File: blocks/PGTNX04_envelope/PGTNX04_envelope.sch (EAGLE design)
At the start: 71 parts, among them IC1 TL084P, IC2 AS3310

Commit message: Committed a load of changes
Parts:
- added STN2: HEADER/MALE/01, connectors:HEADER/MALE/01
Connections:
- new net N$32: R11.S, STN2.3
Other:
- note added: "Connect to STNCV"
- note added: "From STNCV input jack normalled to +V"
- moved on the sheet: R11, R32, STN1, STN3
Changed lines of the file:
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@@
+<attribute name="SPICEPREFIX" value="X"/>
+</part>
+<part name="STN2" library="connectors" deviceset="HEADER/MALE/01" device="">
 <attribute name="SPICEPREFIX" value="X"/>
 </part>
@@
 <sheet>
 <plain>
+<text x="161.29" y="-22.098" size="1.778" layer="95">Connect to STNCV</text>
+<text x="208.28" y="-12.7" size="1.778" layer="95">From STNCV input jack normalled to +V</text>
 </plain>
 <instances>
@@
 <instance part="SUPPLY11" gate="GND" x="55.88" y="-91.44"/>
 <instance part="DCYCV" gate="HEADER" x="83.82" y="-60.96"/>
-<instance part="R11" gate="G$1" x="165.1" y="-17.78" rot="R180"/>
-<instance part="SUPPLY17" gate="GND" x="165.1" y="-27.94"/>
+<instance part="R11" gate="G$1" x="187.96" y="-17.78" rot="R180"/>
+<instance part="SUPPLY17" gate="GND" x="187.96" y="-27.94"/>
 <instance part="STNCV" gate="HEADER" x="152.4" y="-15.24" rot="R270"/>
-<instance part="SUPPLY18" gate="+12V" x="165.1" y="5.08"/>
+<instance part="SUPPLY18" gate="+12V" x="187.96" y="5.08"/>
 <instance part="GATE" gate="HEADER" x="48.26" y="-7.62"/>
 <instance part="GATEN" gate="HEADER" x="48.26" y="-5.08"/>
@@
 <instance part="ATK2" gate="HEADER" x="71.12" y="-190.5" rot="R90"/>
 <instance part="ATK3" gate="HEADER" x="53.34" y="-193.04"/>
-<instance part="R32" gate="G$1" x="165.1" y="-5.08" rot="R90"/>
-<instance part="STN1" gate="HEADER" x="167.64" y="-22.86" rot="R180"/>
-<instance part="STN3" gate="HEADER" x="167.64" y="-12.7" rot="R180"/>
+<instance part="R32" gate="G$1" x="187.96" y="-5.08" rot="R90"/>
+<instance part="STN1" gate="HEADER" x="190.5" y="-22.86" rot="R180"/>
+<instance part="STN3" gate="HEADER" x="190.5" y="-12.7" rot="R180"/>
+<instance part="STN2" gate="HEADER" x="180.34" y="-17.78"/>
 </instances>
 <busses>
@@
 <pinref part="R11" gate="G$1" pin="A"/>
 <pinref part="SUPPLY17" gate="GND" pin="PE"/>
-<wire x1="165.1" y1="-25.4" x2="165.1" y2="-22.86" width="0.1524" layer="91"/>
+<wire x1="187.96" y1="-25.4" x2="187.96" y2="-22.86" width="0.1524" layer="91"/>
 <pinref part="STN1" gate="HEADER" pin="3"/>
-<junction x="165.1" y="-22.86"/>
+<junction x="187.96" y="-22.86"/>
 </segment>
 <segment>
@@
 <pinref part="SUPPLY18" gate="+12V" pin="+12V"/>
 <pinref part="R32" gate="G$1" pin="2"/>
-<wire x1="165.1" y1="2.54" x2="165.1" y2="0" width="0.1524" layer="91"/>
+<wire x1="187.96" y1="2.54" x2="187.96" y2="0" width="0.1524" layer="91"/>
 </segment>
 </net>
@@
 <pinref part="R11" gate="G$1" pin="E"/>
 <pinref part="R32" gate="G$1" pin="1"/>
-<wire x1="165.1" y1="-10.16" x2="165.1" y2="-12.7" width="0.1524" layer="91"/>
+<wire x1="187.96" y1="-10.16" x2="187.96" y2="-12.7" width="0.1524" layer="91"/>
 <pinref part="STN3" gate="HEADER" pin="3"/>
-<junction x="165.1" y="-12.7"/>
-</segment>
-</net>
+<junction x="187.96" y="-12.7"/>
+</segment>
+</net>
+<net name="N$32" class="0">
+<segment>
+<pinref part="R11" gate="G$1" pin="S"/>
+<pinref part="STN2" gate="HEADER" pin="3"/>
+</segment>
+</net>

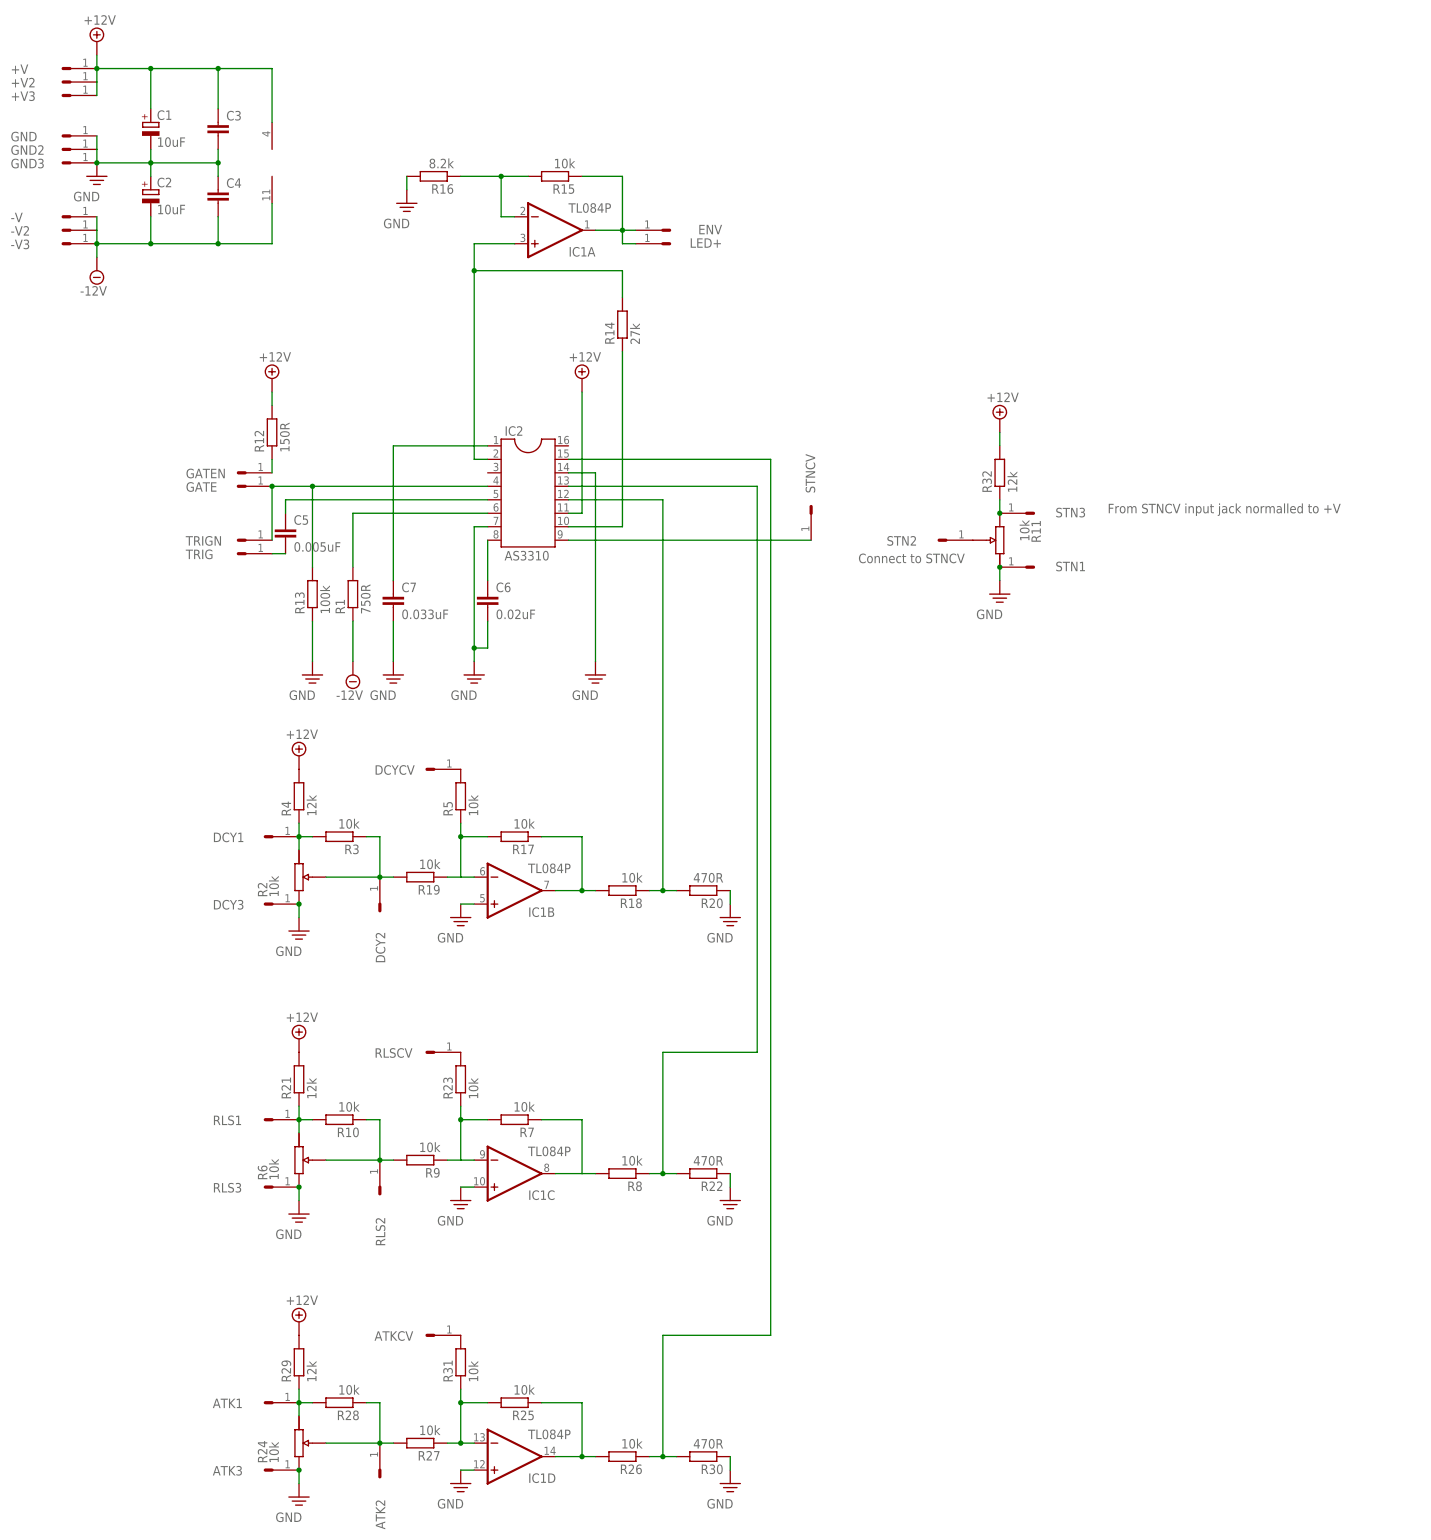
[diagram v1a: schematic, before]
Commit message: Corrected resistor value
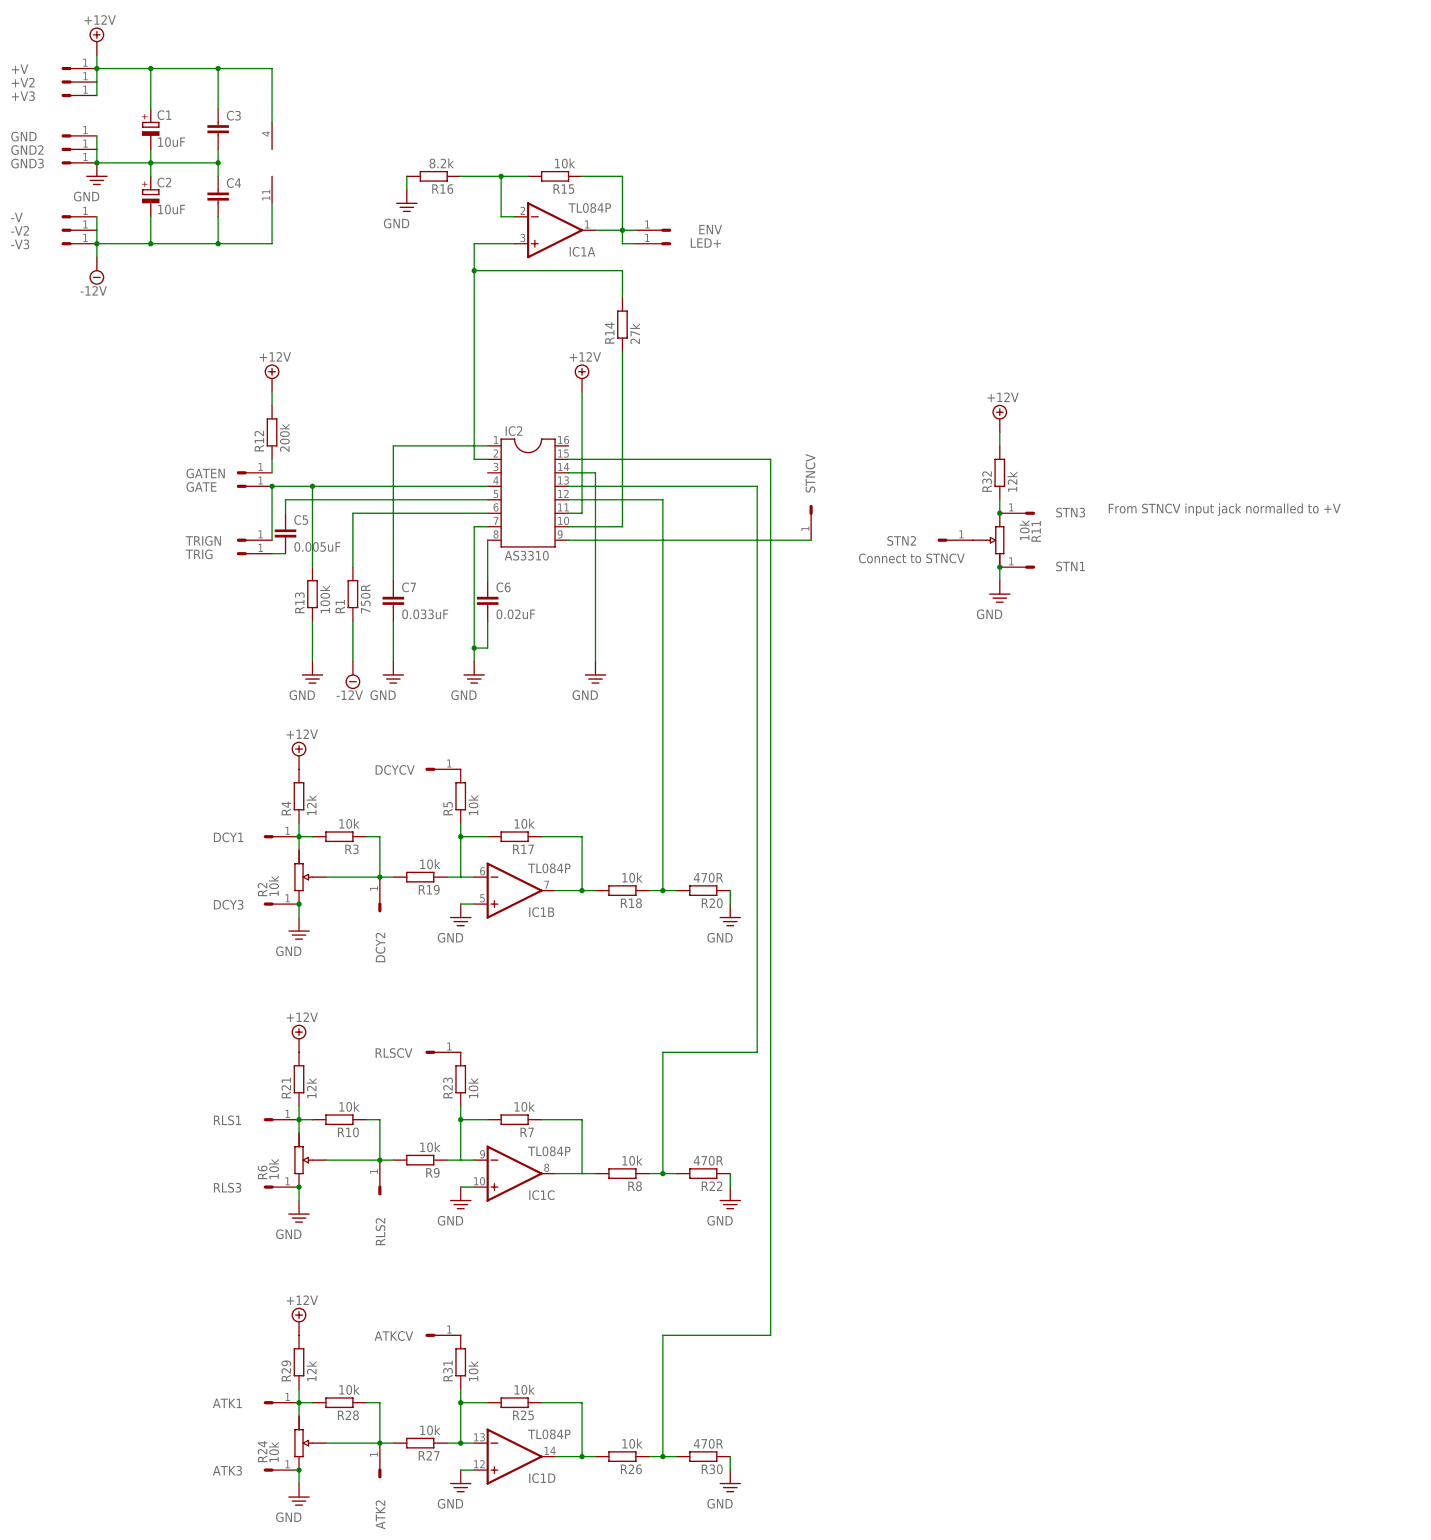
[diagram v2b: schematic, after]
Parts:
- R12: value 150R -> 200k

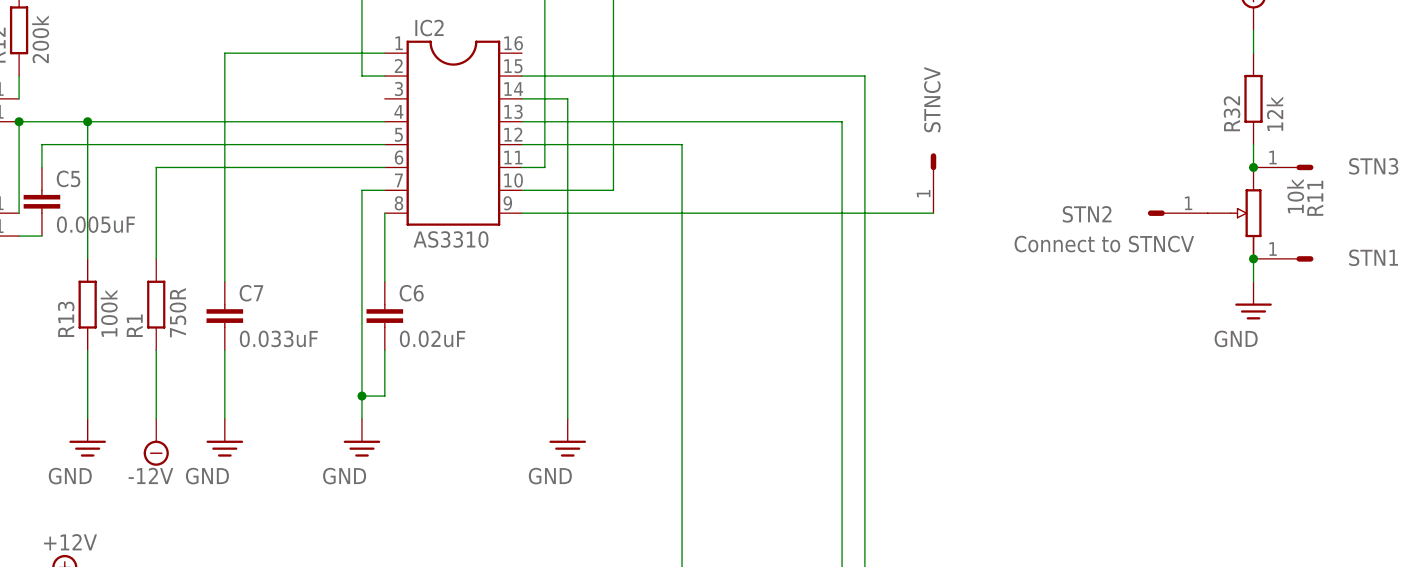
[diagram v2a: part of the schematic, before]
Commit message: Changed resistor value
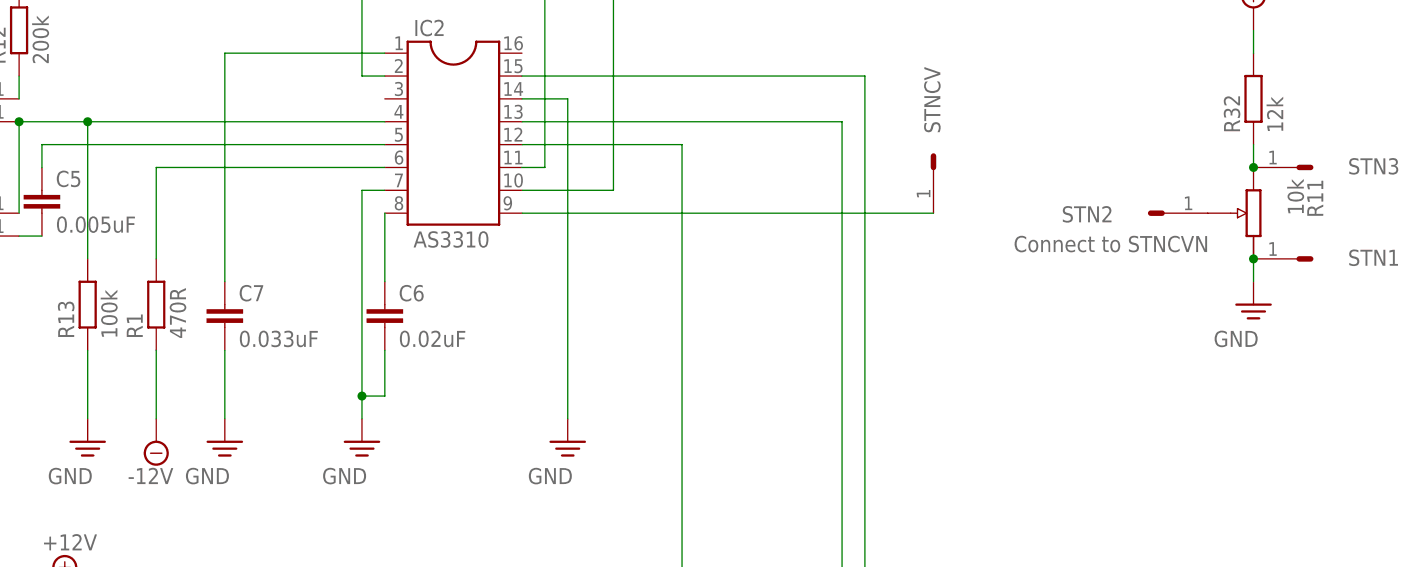
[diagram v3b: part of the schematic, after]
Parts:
- R1: value 750R -> 470R
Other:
- note added: "Connect to STNCVN"
- note removed: "Connect to STNCV"
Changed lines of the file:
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@@
 <?xml version="1.0" encoding="utf-8"?>
 <!DOCTYPE eagle SYSTEM "eagle.dtd">
-<eagle version="9.6.0">
+<eagle version="9.5.0">
 <drawing>
 <settings>
@@
 <part name="C3" library="capacitors" deviceset="CAPACITOR" device="CERAMICDISC/5"/>
 <part name="C4" library="capacitors" deviceset="CAPACITOR" device="CERAMICDISC/5"/>
-<part name="R1" library="resistors" deviceset="RESISTOR" device="RESISTOR/UPRIGHT/7.5" value="750R"/>
+<part name="R1" library="resistors" deviceset="RESISTOR" device="RESISTOR/UPRIGHT/7.5" value="470R"/>
 <part name="SUPPLY7" library="supply" deviceset="-12V" device="">
 <attribute name="SPICEPREFIX" value="G"/>
@@
 <sheet>
 <plain>
-<text x="161.29" y="-22.098" size="1.778" layer="95">Connect to STNCV</text>
+<text x="161.29" y="-22.098" size="1.778" layer="95">Connect to STNCVN</text>
 <text x="208.28" y="-12.7" size="1.778" layer="95">From STNCV input jack normalled to +V</text>
 </plain>

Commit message: Connected C7 to ground
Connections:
- removed net PE: C7.2
- net GND: now also C7.2
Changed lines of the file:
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@@
 <?xml version="1.0" encoding="utf-8"?>
 <!DOCTYPE eagle SYSTEM "eagle.dtd">
-<eagle version="9.5.0">
+<eagle version="9.6.0">
 <drawing>
 <settings>
@@
 <wire x1="88.9" y1="-193.04" x2="86.36" y2="-193.04" width="0.1524" layer="91"/>
 </segment>
+<segment>
+<pinref part="SUPPLY21" gate="GND" pin="PE"/>
+<pinref part="C7" gate="G$1" pin="2"/>
+<wire x1="73.66" y1="-40.64" x2="73.66" y2="-33.02" width="0.1524" layer="91"/>
+</segment>
 </net>
 <net name="+12V" class="0">
@@
 </segment>
 </net>
-<net name="PE" class="0">
-<segment>
-<pinref part="SUPPLY21" gate="GND" pin="PE"/>
-<pinref part="C7" gate="G$1" pin="2"/>
-<wire x1="73.66" y1="-40.64" x2="73.66" y2="-33.02" width="0.1524" layer="91"/>
-</segment>
-</net>
